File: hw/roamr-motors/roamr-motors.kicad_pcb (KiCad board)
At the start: 4 copper layers, 115 x 55 mm, 107 parts, among them J1 JST_XH_S2B-XH-A-1, J10 JST_SH_BM06B-SRSS-TB, J2 USB4215-03-A, J3 USB4215-03-A, J4 JST_XH_S2B-XH-A-1, J5 JST_XH_S2B-XH-A-1, J6 JST_PH_B3B-PH-SM4-TB, J7 JST_SH_BM06B-SRSS-TB, J8 JST_XH_S2B-XH-A-1, J9 JST_PH_B3B-PH-SM4-TB, Q1 L8050QLT1G, Q2 L8050QLT1G, SW1 1825910-6, SW2 1825910-6, U1 SGM2212-3.3XKC3G_TR, U2 CP2102N-A02-GQFN28, U3 ESP32-S3-WROOM-1, U4 DRV8316CRRGFR, U5 DRV8316CRRGFR

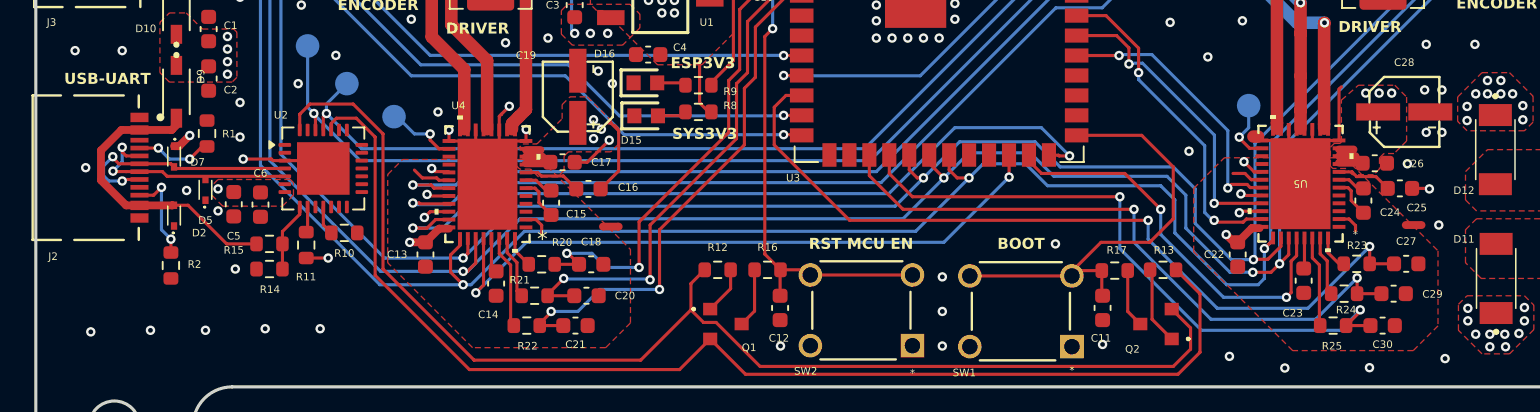
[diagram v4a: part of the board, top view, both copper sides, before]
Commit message: some silkscreen stuff
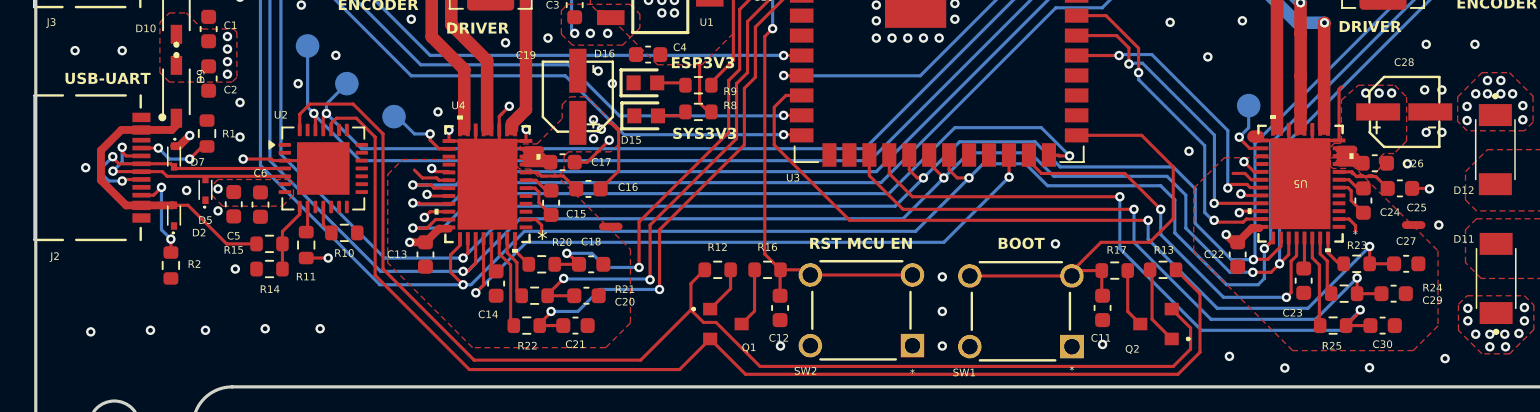
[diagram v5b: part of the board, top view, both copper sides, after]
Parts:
- moved J2 0.12 mm to (92.8, 100.8)
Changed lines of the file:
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@@
 	(footprint "USB4215_03_A:CONN_8p94X6p5X3p16_12L_GCC"
 		(layer "F.Cu")
-		(at 92.67608 100.85 -90)
+		(at 92.8 100.85 -90)
 		(tags "USB4215-03-A ")
 		(property "Reference" "J2"
@@
 		(tags "capacitor")
 		(property "Reference" "C20"
-			(at 2.45 0 0)
+			(at 2.45 0.4 0)
 			(layer "F.SilkS")
 			(effects
@@
 		(tags "resistor")
 		(property "Reference" "R21"
-			(at -0.95 -1 0)
+			(at 5.75 -0.4 0)
 			(layer "F.SilkS")
 			(effects
@@
 		(tags "capacitor")
 		(property "Reference" "C29"
-			(at 2.475 0.032567 0)
+			(at 2.475 0.432567 0)
 			(layer "F.SilkS")
 			(effects
@@
 		(tags "resistor")
 		(property "Reference" "R24"
-			(at 0.125 1.032567 0)
+			(at 5.625 -0.367433 0)
 			(layer "F.SilkS")
 			(effects

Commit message: i don't remember what this change was but probably fuses?
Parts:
- added F1: 0466005.NRHF, 0466005:F1206, F.Cu at (190.7, 100.8)
- added F2: 0466005.NRHF, 0466005:F1206, F.Cu at (190.7, 107.3)
- moved NT2 8.20 mm to (177.0, 112.7), turned to -90 degrees
- moved C28 2.95 mm to (175.2, 94.7), turned to 90 degrees
- moved C27 2.60 mm to (174.7, 105.3)
- moved D1 2.50 mm to (185.9, 98.8)
- moved D4 2.50 mm to (185.9, 109.0)
- moved D11 2.45 mm to (180.0, 107.9)
- moved D12 2.40 mm to (180.0, 99.7)
- moved C25 1.03 mm to (175.6, 102.9), turned to -90 degrees
- moved R23 0.35 mm to (173.2, 107.0)
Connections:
- J1 pad 1: VIN_12V -> Net-(J1-Pin_1)
- J4 pad 1: VIN_5V -> Net-(J4-Pin_1)
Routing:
- net GND: track 50.2 -> 47.6 mm, vias 120 -> 116
- net /BLDC Driver 2/AGND: track 3.57 -> 5.73 mm
- net VSYS_12V: track 14.6 -> 14.8 mm, vias 27 -> 21
- net VSYS_5V: vias 24 -> 20
- added copper zone on F.Cu, net Net-(J1-Pin_1)
- added copper zone on F.Cu, net Net-(J4-Pin_1)
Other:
- board text added: "5A FUSE"

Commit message: drc
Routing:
- net VSYS_3V3: track 53.0 -> 53.6 mm
- net GND: track 47.6 -> 47.9 mm, vias 116 -> 120
- removed copper zone on In2.Cu, net GND
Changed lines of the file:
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@@
 	)
 	(segment
+		(start 105.35 102.4)
+		(end 105.35 102.15)
+		(width 0.5)
+		(layer "F.Cu")
+		(net 2)
+	)
+	(segment
 		(start 167.549811 102.617622)
 		(end 167.5489 102.617622)
@@
 	)
 	(segment
+		(start 105.3 102.1)
+		(end 105 102.1)
+		(width 0.5)
+		(layer "F.Cu")
+		(net 2)
+	)
+	(segment
 		(start 166.2 102.517433)
 		(end 166.4 102.517433)
@@
 	)
 	(segment
+		(start 105.35 102.15)
+		(end 105.3 102.1)
+		(width 0.5)
+		(layer "F.Cu")
+		(net 2)
+	)
+	(segment
 		(start 114.601029 103.650441)
 		(end 114.234434 104.017036)
@@
 	)
 	(segment
+		(start 97.96 104.56)
+		(end 97.7 104.3)
+		(width 0.5)
+		(layer "F.Cu")
+		(net 54)
+	)
+	(segment
 		(start 117.499622 101.149811)
 		(end 118.249811 101.9)
@@
 	)
 	(via
+		(at 166.1 95.6)
+		(size 0.6)
+		(drill 0.3)
+		(layers "F.Cu" "B.Cu")
+		(free yes)
+		(net 54)
+	)
+	(via
 		(at 165.4757 112.859579)
 		(size 0.6)
@@
 	)
 	(via
-		(at 196.4 96.8)
+		(at 197.2 96.7)
 		(size 0.6)
 		(drill 0.3)
@@
 	)
 	(via
+		(at 115.7 96.4)
+		(size 0.6)
+		(drill 0.3)
+		(layers "F.Cu" "B.Cu")
+		(free yes)
+		(net 54)
+	)
+	(via
 		(at 182.8 112.5)
 		(size 0.6)
@@
 	)
 	(via
+		(at 173 96.5)
+		(size 0.6)
+		(drill 0.3)
+		(layers "F.Cu" "B.Cu")
+		(free yes)
+		(net 54)
+	)
+	(via
 		(at 147.2 110)
 		(size 0.6)
@@
 	)
 	(via
-		(at 199.4 87.6)
+		(at 199.2 87.6)
 		(size 0.6)
 		(drill 0.3)
@@
 	)
 	(via
+		(at 173 97.8)
+		(size 0.6)
+		(drill 0.3)
+		(layers "F.Cu" "B.Cu")
+		(free yes)
+		(net 54)
+	)
+	(via
 		(at 165.4 84.7)
 		(size 0.6)
@@
 	)
 	(via
-		(at 92.67608 100.85)
+		(at 121.6 98)
 		(size 0.6)
 		(drill 0.3)
@@
 	)
 	(via
-		(at 200 108.4)
+		(at 92.67608 100.85)
 		(size 0.6)
 		(drill 0.3)
@@
 	)
 	(via
-		(at 192.5 79.5)
+		(at 200 108.4)
 		(size 0.6)
 		(drill 0.3)
@@
 	)
 	(via
-		(at 148 88.4)
+		(at 192.5 79.5)
 		(size 0.6)
 		(drill 0.3)
@@
 	)
 	(via
-		(at 115.8 98.4544)
+		(at 148 88.4)
 		(size 0.6)
 		(drill 0.3)
 		(layers "F.Cu" "B.Cu")
+		(free yes)
 		(net 54)
 	)
@@
 	)
 	(via
+		(at 165.5 97.7)
+		(size 0.6)
+		(drill 0.3)
+		(layers "F.Cu" "B.Cu")
+		(free yes)
+		(net 54)
+	)
+	(via
 		(at 119.640097 96.940098)
 		(size 0.6)
@@
 	)
 	(via
-		(at 194.7 87.4)
+		(at 194.2 87.8)
 		(size 0.6)
 		(drill 0.3)
@@
 	)
 	(via
-		(at 115.1 97.3)
-		(size 0.6)
-		(drill 0.3)
-		(layers "F.Cu" "B.Cu")
-		(free yes)
-		(net 54)
-	)
-	(via
 		(at 176.5 101)
 		(size 0.6)
@@
 	)
 	(via
-		(at 198.2 97.1)
+		(at 199.7 98.7)
 		(size 0.6)
 		(drill 0.3)
@@
 	)
 	(via
-		(at 109.3 76.5)
+		(at 122.1 97)
 		(size 0.6)
 		(drill 0.3)
@@
 	)
 	(via
-		(at 100.3 77.4)
+		(at 109.3 76.5)
 		(size 0.6)
 		(drill 0.3)
@@
 	)
 	(via
-		(at 194.2 105.9)
+		(at 100.3 77.4)
 		(size 0.6)
 		(drill 0.3)
@@
 	)
 	(via
-		(at 145 92.6)
+		(at 194.2 105.9)
 		(size 0.6)
 		(drill 0.3)
@@
 	)
 	(via
-		(at 194.2 96.6)
+		(at 145 92.6)
 		(size 0.6)
 		(drill 0.3)
@@
 	)
 	(via
-		(at 120.711397 98.415797)
+		(at 194.5 96.9)
 		(size 0.6)
 		(drill 0.3)
 		(layers "F.Cu" "B.Cu")
+		(free yes)
 		(net 54)
 	)
@@
 	)
 	(zone
-		(net 54)
-		(net_name "GND")
-		(layer "In2.Cu")
-		(hatch edge 0.5)
-		(connect_pads
-			(clearance 0.5)
-		)
-		(min_thickness 0.25)
-		(filled_areas_thickness no)
-		(fill yes
-			(thermal_gap 0.5)
-			(thermal_bridge_width 0.5)
-		)
-		(polygon
-			(pts
-				(arc
-					(start 92.898182 72.309137)
-					(mid 96.098182 72.309137)
-					(end 92.898182 72.309137)
-				)
-			)
-		)
-	)
-	(zone
 		(net 4)
 		(net_name "VSYS_5V")
@@
 	)
 	(zone
-		(net 54)
-		(net_name "GND")
-		(layer "In2.Cu")
-		(hatch edge 0.5)
-		(connect_pads
-			(clearance 0.5)
-		)
-		(min_thickness 0.25)
-		(filled_areas_thickness no)
-		(fill yes
-			(thermal_gap 0.5)
-			(thermal_bridge_width 0.5)
-		)
-		(polygon
-			(pts
-				(arc
-					(start 197.898182 72.309137)
-					(mid 201.098182 72.309137)
-					(end 197.898182 72.309137)
-				)
-			)
-		)
-	)
-	(zone
-		(net 54)
-		(net_name "GND")
-		(layer "In2.Cu")
-		(hatch edge 0.5)
-		(connect_pads
-			(clearance 0.5)
-		)
-		(min_thickness 0.25)
-		(filled_areas_thickness no)
-		(fill yes
-			(thermal_gap 0.5)
-			(thermal_bridge_width 0.5)
-		)
-		(polygon
-			(pts
-				(arc
-					(start 92.898182 117.309137)
-					(mid 96.098182 117.309137)
-					(end 92.898182 117.309137)
-				)
-			)
-		)
-	)
-	(zone
 		(net 2)
 		(net_name "VSYS_3V3")
@@
 		)
 	)
-	(zone
-		(net 54)
-		(net_name "GND")
-		(layer "In2.Cu")
-		(hatch edge 0.5)
-		(connect_pads
-			(clearance 0.5)
-		)
-		(min_thickness 0.25)
-		(filled_areas_thickness no)
-		(fill yes
-			(thermal_gap 0.5)
-			(thermal_bridge_width 0.5)
-		)
-		(polygon
-			(pts
-				(arc
-					(start 197.898182 117.309137)
-					(mid 201.098182 117.309137)
-					(end 197.898182 117.309137)
-				)
-			)
-		)
-	)
 	(group ""
 		(members "581ee530-94f5-4719-bb7d-86b98d0db403")
@@
 	)
 	(group ""
-		(members "0d5c7cfb-67a4-4b00-aed7-2cd9d9a77d2e" "22a7ee31-b4d4-4d35-bc57-13ee3ee066c1"
-			"25f6a638-9f6e-401c-9a3e-adda958f1c51" "3c205f3f-967c-466e-aa64-d88948ab6cc1"
-			"8badd049-96af-44e1-820c-60af81437b43"
-		)
+		(members "22a7ee31-b4d4-4d35-bc57-13ee3ee066c1")
 	)
 	(group ""

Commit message: outputs and last minute updates
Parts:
- added G***: LOGO, LOGO, F.Cu at (163.4, 92.2)
- D1, D4: value SMLJ12A-R -> SMLJ13CA-R; footprint SMLJ12A-R:DIOM7959X262N -> SMLJ13CA-R:DIOM7959X262N
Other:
- board text added: "BLDC Motors V1 Designed by Olivia Ye and Thomason Zhou 2/21/2026"
- board text added: "roamr"
